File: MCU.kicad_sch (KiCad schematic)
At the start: 1 part, among them U2 STM32G474CEUx

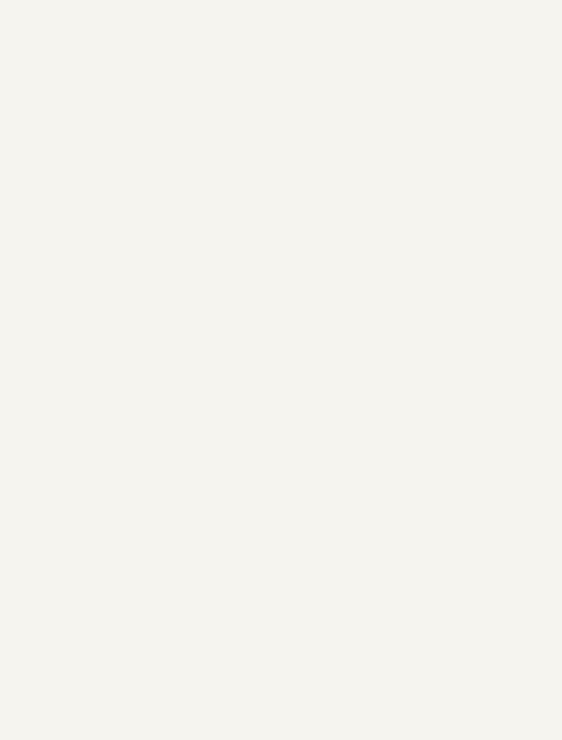
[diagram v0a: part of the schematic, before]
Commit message: Cleaned up the hierarchy
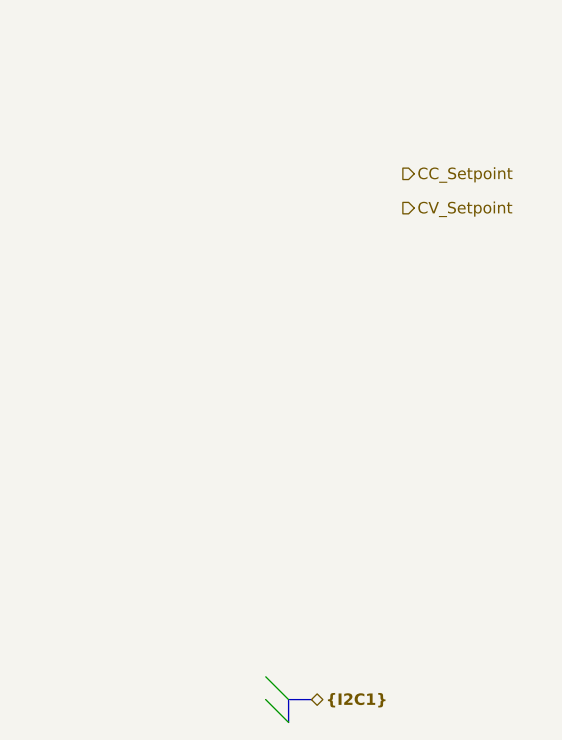
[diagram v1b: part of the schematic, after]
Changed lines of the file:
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@@
 	(generator_version "10.0")
 	(paper "A4")
+	(bus_entry
+		(at 96.52 166.37)
+		(size 2.54 2.54)
+		(stroke
+			(width 0)
+			(type default)
+		)
+	)
+	(bus_entry
+		(at 96.52 163.83)
+		(size 2.54 2.54)
+		(stroke
+			(width 0)
+			(type default)
+		)
+	)
+	(bus
+		(pts
+			(xy 99.06 166.37) (xy 99.06 168.91)
+		)
+		(stroke
+			(width 0)
+			(type default)
+		)
+	)
+	(bus
+		(pts
+			(xy 99.06 166.37) (xy 101.6 166.37)
+		)
+		(stroke
+			(width 0)
+			(type default)
+		)
+	)
+	(hierarchical_label "CC_Setpoint"
+		(shape output)
+		(at 111.76 107.95 0)
+		(effects
+			(font
+				(size 1.27 1.27)
+			)
+			(justify left)
+		)
+	)
+	(hierarchical_label "{I2C1}"
+		(shape bidirectional)
+		(at 101.6 166.37 0)
+		(effects
+			(font
+				(size 1.27 1.27)
+				(thickness 0.254)
+				(bold yes)
+				(color 0 0 0 1)
+			)
+			(justify left)
+		)
+	)
+	(hierarchical_label "CV_Setpoint"
+		(shape output)
+		(at 111.76 111.76 0)
+		(effects
+			(font
+				(size 1.27 1.27)
+			)
+			(justify left)
+		)
+	)
 	(symbol
 		(lib_id "MCU_ST_STM32G4:STM32G474CEUx")

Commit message: inductor, output fets
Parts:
- added C65, C67, C68, C69: 100nF, Capacitor_SMD:C_0402_1005Metric, symbol Device:C_Small
- added C66, C70: 10uF, Capacitor_SMD:C_1210_3225Metric, symbol Device:C_Small
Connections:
- net +3V3: now reaches U2.1 (VBAT)
- net +3V3: now also U2.20 (VREF+), U2.21 (VDDA), U2.23 (VDD), U2.35 (VDD), U2.48 (VDD), C65.1, C66.1, C67.1, C68.1, C69.1, C70.1
- net GND: now reaches U2.49 (VSS)
- net GND: now also C65.2, C66.2, C67.2, C68.2, C69.2, C70.2
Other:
- moved on the sheet: U2

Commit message: Starting with layout, oled, encoder, xt90
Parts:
- added C71, C72, C73, C74, C78: 100nF, Capacitor_SMD:C_0402_1005Metric, symbol Device:C_Small
- added C75, C76: 15pF, Capacitor_SMD:C_0603_1608Metric, symbol Device:C_Small
- added C77: 10uF, Capacitor_SMD:C_1210_3225Metric, symbol Device:C_Small
- added D15: APTD1608LQBC/D, Altium_port:kingbright_0603_blue, symbol 0_PD240W:APTD1608LQBC/D
- added J4: SWD, Connector:Tag-Connect_TC2030-IDC-NL_2x03_P1.27mm_Vertical, symbol Connector_Generic:Conn_02x03_Odd_Even
- added J5: SSD1306, thommys-parts2:ssd13062, symbol Connector_Generic:Conn_01x04
- added R58: 330R 1%, Resistor_SMD:R_0402_1005Metric, symbol 0_passives:R_0402
- added R59: 357k, Resistor_SMD:R_0402_1005Metric, symbol Device:R_Small
- added SW1: EC11E15244G1, thommys-parts2:RotaryEncoder_Alps_EC11E-Switch_Vertical_H20mm, symbol Device:RotaryEncoder_Switch_MP
- added U12: FT234XD, Package_DFN_QFN:WDFN-12-1EP_3x3mm_P0.45mm_EP1.7x2.5mm, symbol Interface_USB:FT234XD
- added Y1: 8M, Crystal:Crystal_SMD_3225-4Pin_3.2x2.5mm, symbol Device:Crystal_GND24
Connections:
- net +3V3: now also U2.7 (PG10), C71.1, C72.1, C77.1, C78.1, D15.2 (A), J4.1 (Pin_1), J5.1 (Pin_1), U12.4 (VCC)
- net CC_Setpoint: now also U2.14 (PA6)
- net CV_Setpoint: now also U2.12 (PA4)
- net Current_Feedback: now also U2.11 (PA3)
- net GND: now also C71.2, C72.2, C73.2, C74.2, C75.2, C76.2, C77.2, C78.2, J4.5 (Pin_5), J5.2 (Pin_2), R59.2, SW1.MP, U12.13 (GND), U12.5 (GND), Y1.2 (G), Y1.4 (G)
- net Bus voltage: now reaches U2.15 (PA7)
- net I2CC_SDA_MCU: now reaches U2.16 (PC4)
- net I2CC_SDA_MCU: now also J5.4 (Pin_4)
- net I2CC_SCL_MCU: now reaches U2.30 (PA8)
- net I2CC_SCL_MCU: now also J5.3 (Pin_3)
- net Temp: now reaches U2.31 (PA9)
- net SWDIO: now reaches U2.36 (PA13)
- net SWDIO: now also J4.2 (Pin_2)
- net SWCLK: now reaches U2.37 (PA14)
- net SWCLK: now also J4.4 (Pin_4)
- net at U2.39 (PC10): now also U12.7 (TXD/D0)
- net at U2.40 (PC11): now also U12.10 (RXD/D1)
- net at U2.46 (PB8): now also R59.1
- net at U2.5 (PF0): now also C75.1, Y1.1
- net at U2.6 (PF1): now also C76.1, Y1.3
- new net: D15.1 (C), R58.1
- new net: C73.1, C74.1, U12.2 (~{RESET}), U12.3 (3V3OUT), U12.9 (VCCIO)
- new net: R58.2, U12.6 (CBUS0)
- new net USB_D_N: U12.1 (USBDM)
- new net USB_D_P: U12.12 (USBDP)
- no-connect marks 0 -> 2
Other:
- moved on the sheet: C65, C66, C67, C68, C69, C70, U2

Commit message: Finished layout
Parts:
- added C79, C80: 1nF, Capacitor_SMD:C_0402_1005Metric, symbol Device:C_Small
- added C81, C82, C83, C84: 100nF, Capacitor_SMD:C_0402_1005Metric, symbol Device:C_Small
- added R53, R61, R62, R63, R64, R67, R69, R71: 10k, Resistor_SMD:R_0402_1005Metric, symbol Device:R_Small
- added R65, R66, R68, R70: 1k, Resistor_SMD:R_0402_1005Metric, symbol Device:R_Small
- added S1, S2, S3: Tactile Button, 160gf, PCM_JLCPCB:SW-SMD_4P-L5.1-W5.1-P3.70-LS6.5-TL-2, symbol PCM_JLCPCB-Connectors_Buttons:Tactile Button, 160gf, 12V, 50mA, 5.1mm
- C75, C76: value 15pF -> 22pF; LCSC C1644 -> (none)
- J4, J5: now left out of the parts list
- U12: JLC (none) -> C132158
- U2: JLC (none) -> C1235412
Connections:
- net +3V3: now also R53.1, R61.1, R64.1, R67.1, R69.1, R71.1
- net GND: now also SW1.C, SW1.S2, C79.2, C80.2, C81.2, C82.2, C83.2, C84.2, S1.3 (C), S2.3 (C), S3.3 (C)
- net at SW1.A: now also C79.1, R53.2, R62.1
- net at SW1.B: now also C80.1, R61.2, R63.1
- net at SW1.S1: now also C81.1, R64.2, R65.1
- net BUTT_2: now reaches U2.22 (PB10)
- net BUTT_2: now also R68.2
- net BUTT_3: now reaches U2.24 (PB11)
- net BUTT_3: now also R70.2
- net PD_GPIO3: now reaches U2.25 (PB12)
- net USB_PD_IRQ: now reaches U2.26 (PB13)
- net SWITCH_EN_READ: now reaches U2.27 (PB14)
- net PD_GPIO1: now reaches U2.28 (PB15)
- net Temp Converter: now reaches U2.32 (PA10)
- net SWITCH_EN_MANUAL: now reaches U2.41 (PB3)
- net ENC_A: now reaches U2.42 (PB4)
- net ENC_A: now also R62.2
- net ENC_B: now reaches U2.43 (PB5)
- net ENC_B: now also R63.2
- net ENC_BUTT: now reaches U2.44 (PB6)
- net ENC_BUTT: now also R65.2
- net BUTT_1: now reaches U2.47 (PB9)
- net BUTT_1: now also R66.2
- net Temp renamed Temp PWR In
- new net: C83.1, R68.1, R69.2, S2.1 (A)
- new net: C84.1, R70.1, R71.2, S3.1 (A)
- new net: C82.1, R66.1, R67.2, S1.1 (A)
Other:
- moved on the sheet: C65, C66, C67, C68, C69, C70, C71, C72, C73, C74, C75, C76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

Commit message: Started routing
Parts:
- added Q13: AO3404A, Altium_port:sot-23-3L_103p_300x130x110_n, symbol Transistor_FET_Other:Q_NMOS_Depletion_GSD
- added R78: 10, Resistor_SMD:R_0402_1005Metric, symbol Device:R_Small
- added R79: 1k, Resistor_SMD:R_0402_1005Metric, symbol Device:R_Small
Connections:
- net +3V3: now also R79.2
- net GND: now also Q13.2 (S)
- net at U2.33 (PA11): now also R78.1
- net Vsense_REG_OUT: now reaches U2.34 (PA12)
- new net: Q13.1 (G), R78.2, R79.1
- new net Converter-Disable: Q13.3 (D)
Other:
- title: (none) -> Nitride-Nano
- moved on the sheet: C65, C66, C67, C68, C69, C70, C71, C72, C73, C74, C75, C76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

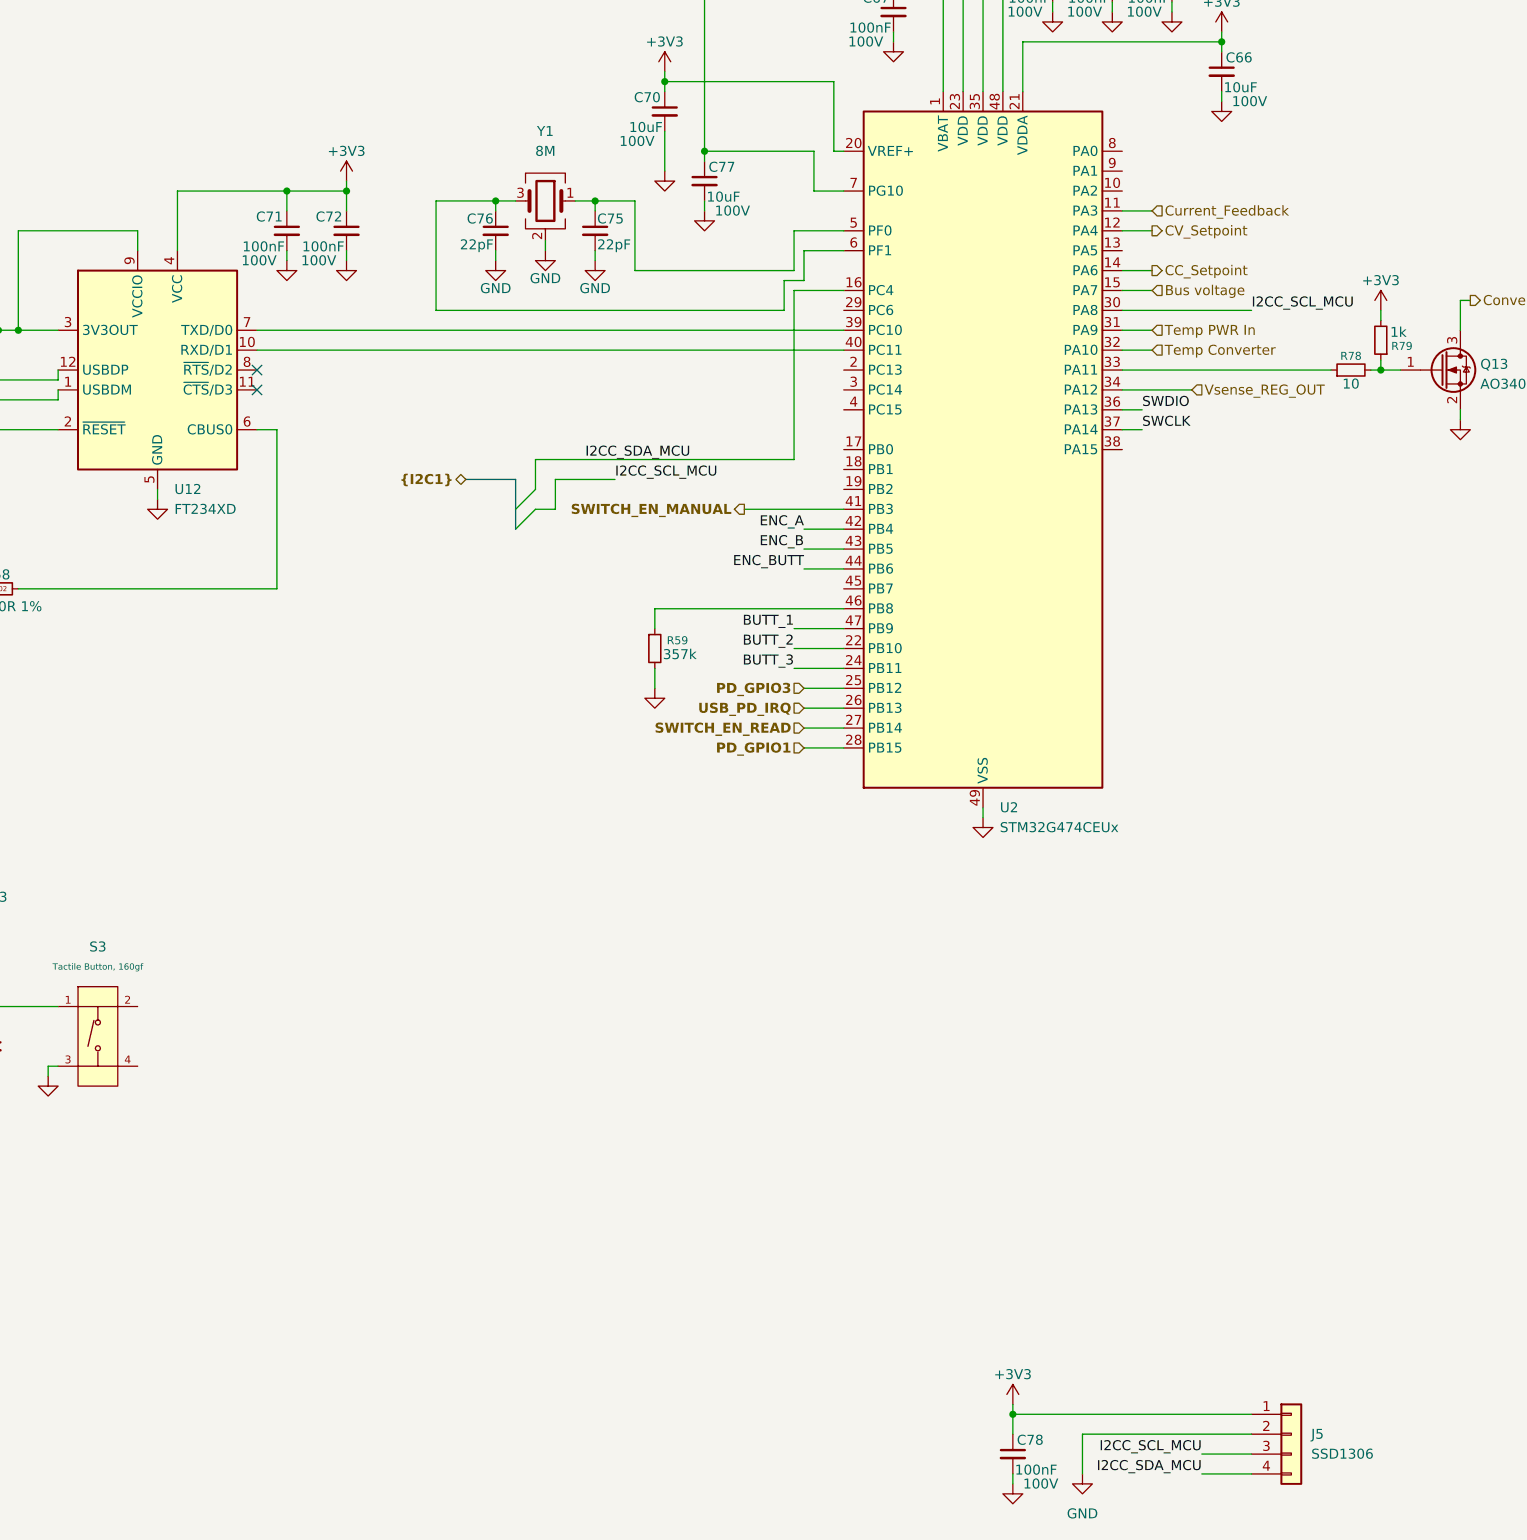
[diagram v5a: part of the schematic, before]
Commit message: fixed pinout of cpu, added freecad file for the housing
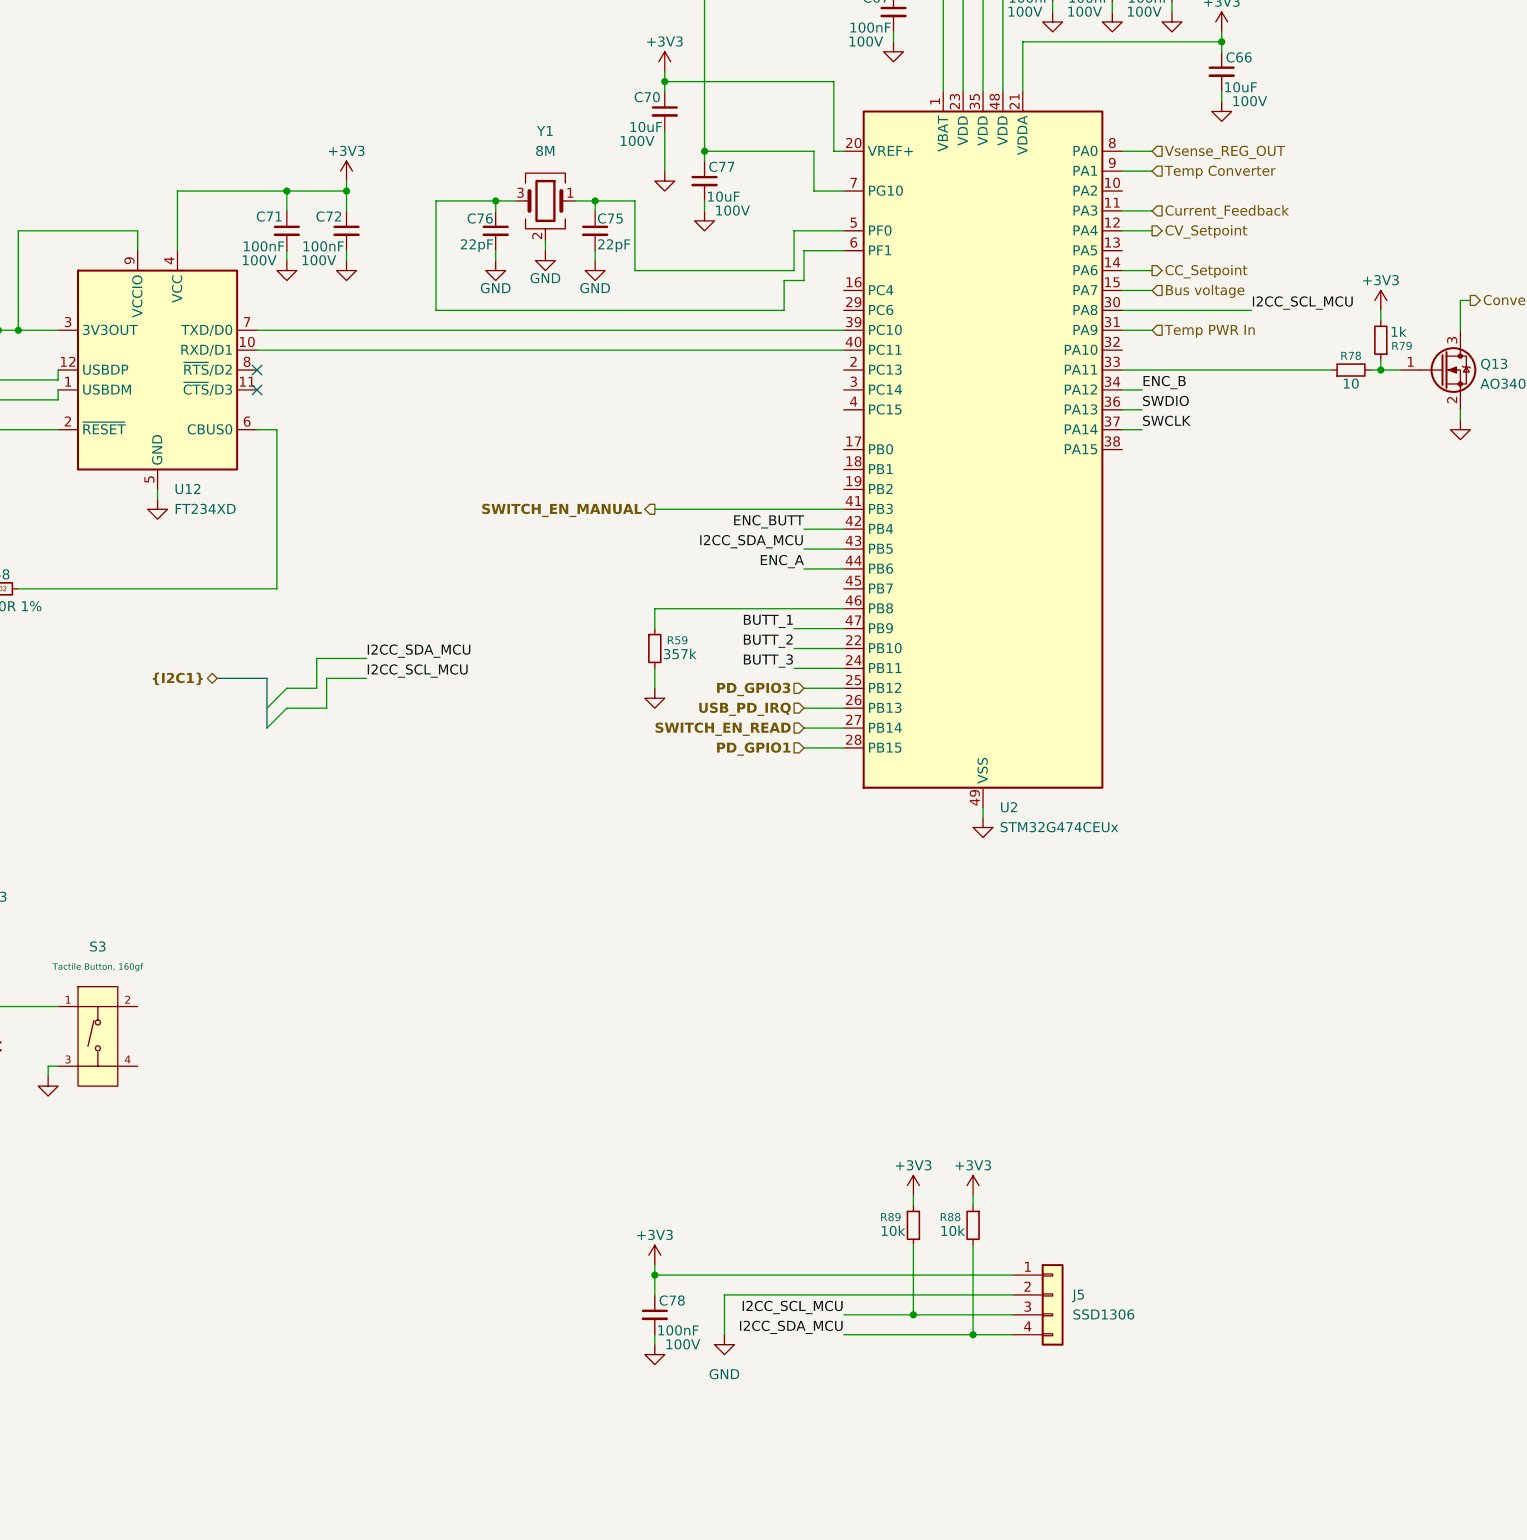
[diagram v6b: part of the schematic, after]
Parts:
- added R88, R89: 10k, Resistor_SMD:R_0402_1005Metric, symbol Device:R_Small
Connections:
- net +3V3: now also R88.1, R89.1
- net ENC_A: now also U2.44 (PB6); no longer U2.42 (PB4)
- net ENC_B: now also U2.34 (PA12); no longer U2.43 (PB5)
- net ENC_BUTT: now also U2.42 (PB4); no longer U2.44 (PB6)
- net I2CC_SCL_MCU: now also R89.2
- net I2CC_SDA_MCU: now also U2.43 (PB5), R88.2; no longer U2.16 (PC4)
- net Temp Converter: now also U2.9 (PA1); no longer U2.32 (PA10)
- net Vsense_REG_OUT: now also U2.8 (PA0); no longer U2.34 (PA12)
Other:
- moved on the sheet: C78, J5

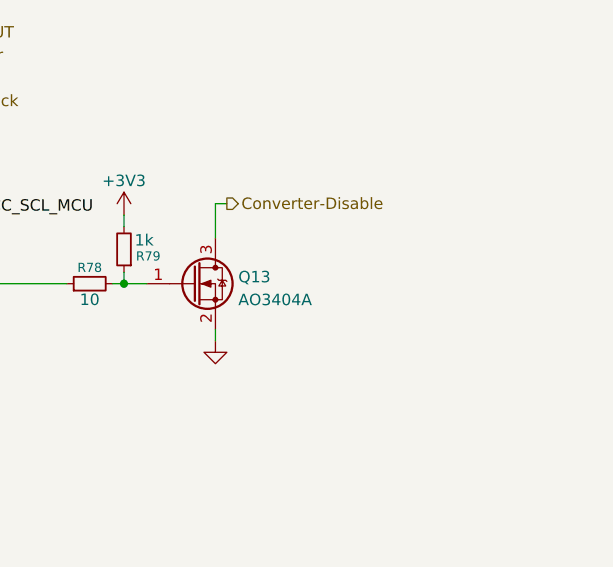
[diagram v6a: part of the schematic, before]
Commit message: Added 5V fan psu
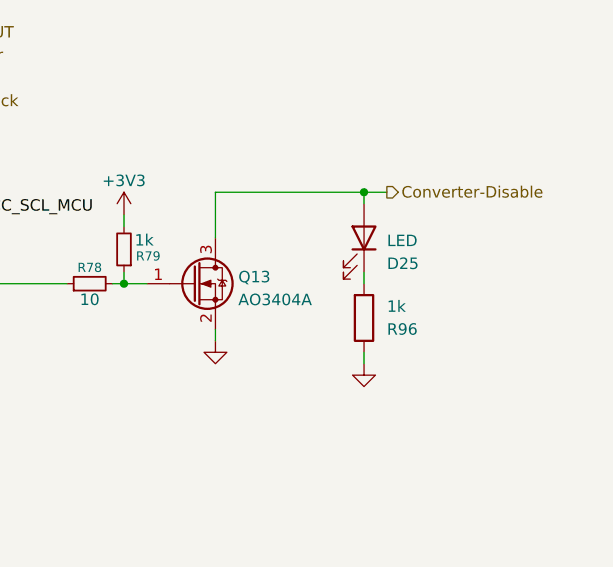
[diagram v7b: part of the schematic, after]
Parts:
- added D25: LED, LED_SMD:LED_0603_1608Metric, symbol Device:LED
- added R96: 1k, Resistor_SMD:R_0402_1005Metric, symbol Device:R
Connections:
- net Converter-Disable: now also D25.2 (A)
- net GND: now also R96.1
- new net: D25.1 (K), R96.2
